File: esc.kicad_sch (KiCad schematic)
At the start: 58 parts, among them Q10 NMOS, Q5 NMOS, Q6 NMOS, Q7 NMOS, Q8 NMOS, Q9 NMOS, U16 DRV8328ARUYR, U20 STM32G071GBU6

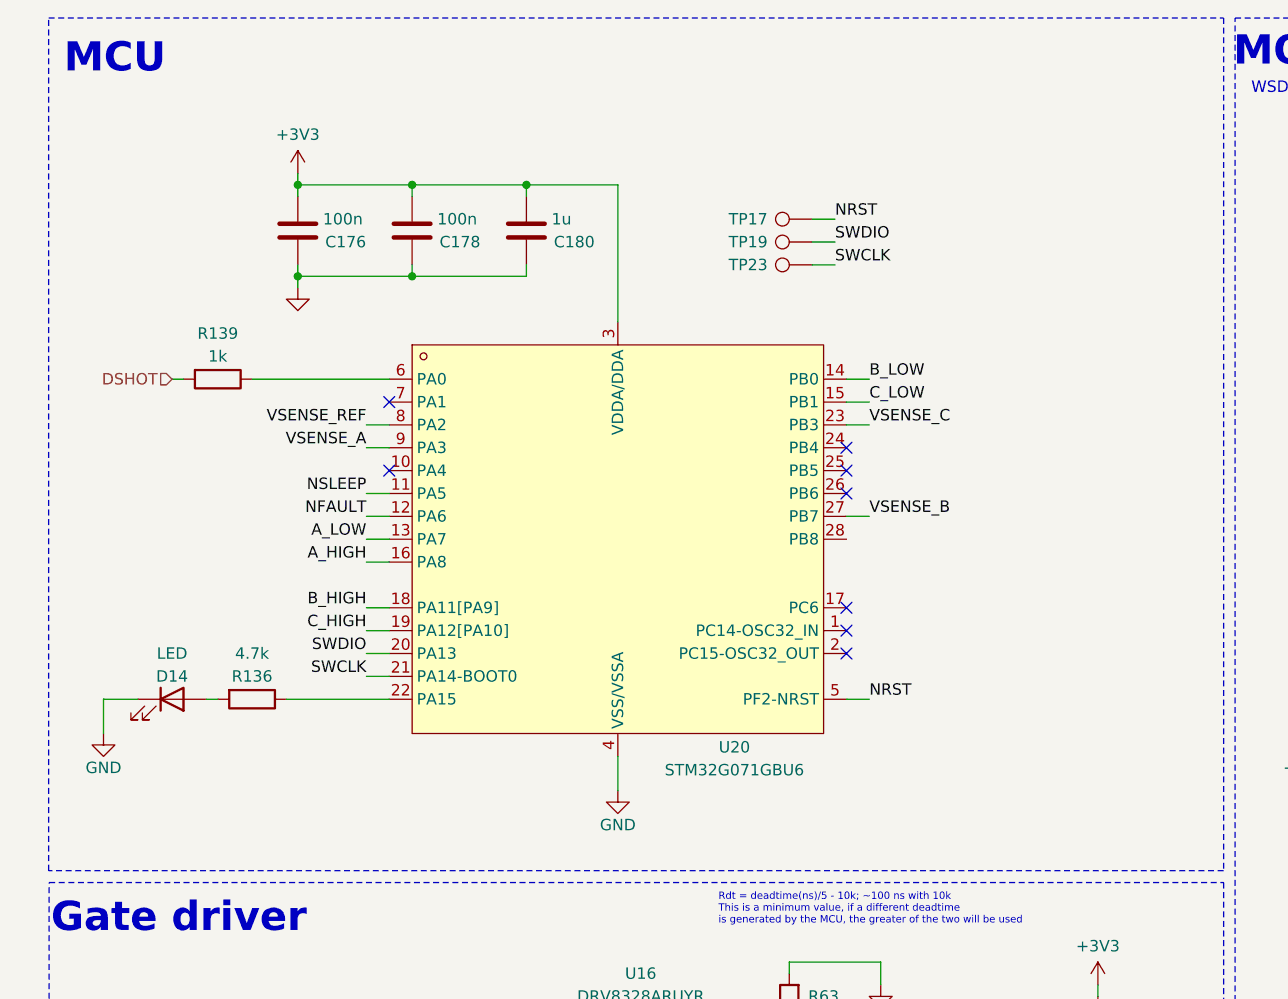
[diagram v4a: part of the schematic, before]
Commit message: Ostensibly finish V4 ESC layout
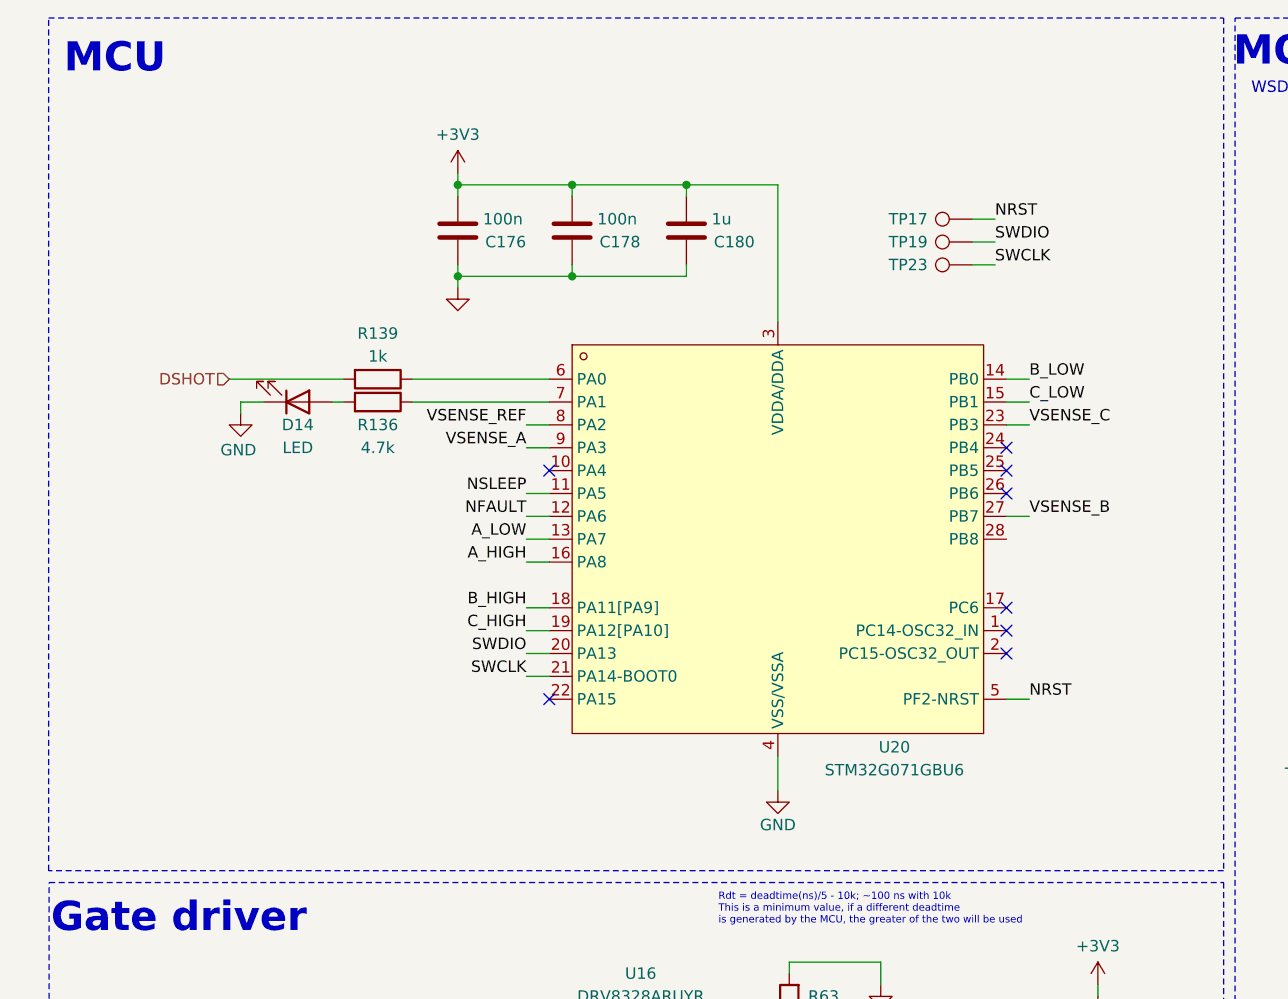
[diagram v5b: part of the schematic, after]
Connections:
- net at U20.22 (PA15): no longer R136.1
- net at U20.7 (PA1): now also R136.1
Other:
- moved on the sheet: C176, C178, C180, D14, R136, R139, TP17, TP19, TP23, U20

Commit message: Remove extra capacitors for now
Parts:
- removed C116, C118, C120, C122, C123, C124, C125, C202, C206: 10u, Capacitor_SMD:C_1206_3216Metric, symbol Device:C
- C113, C114, C121, C198: footprint Capacitor_SMD:C_1206_3216Metric -> Capacitor_SMD:C_1210_3225Metric
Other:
- moved on the sheet: C113, C114, C121, C198

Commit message: Group FC stuff
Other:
- note added: "1210 10uF caps from Samsung retain ~8 uF even at 3S LiHV Which results in ~32 uF total in the worst case scenario"
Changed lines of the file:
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@@
+		)
+	)
+	(text "1210 10uF caps from Samsung retain ~8 uF even at 3S LiHV\nWhich results in ~32 uF total in the worst case scenario"
+		(exclude_from_sim no)
+		(at 219.71 153.924 0)
+		(effects
+			(font
+				(size 1.27 1.27)
+			)
 		)
 	)

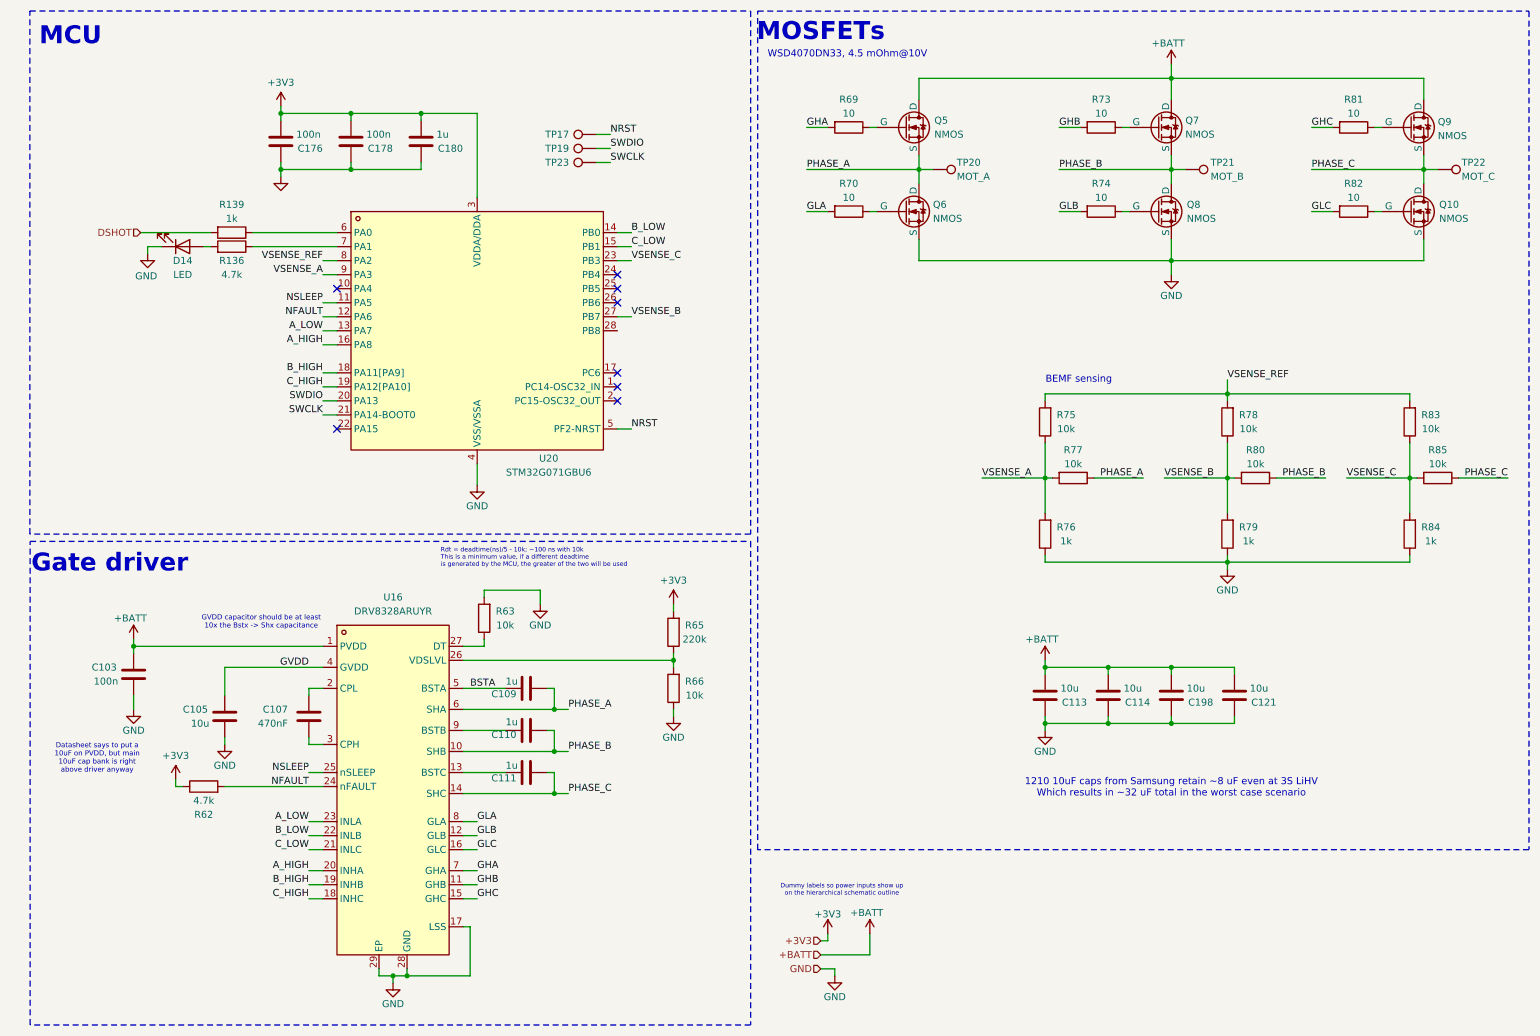
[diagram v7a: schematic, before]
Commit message: Fix BEMF comparator pinout
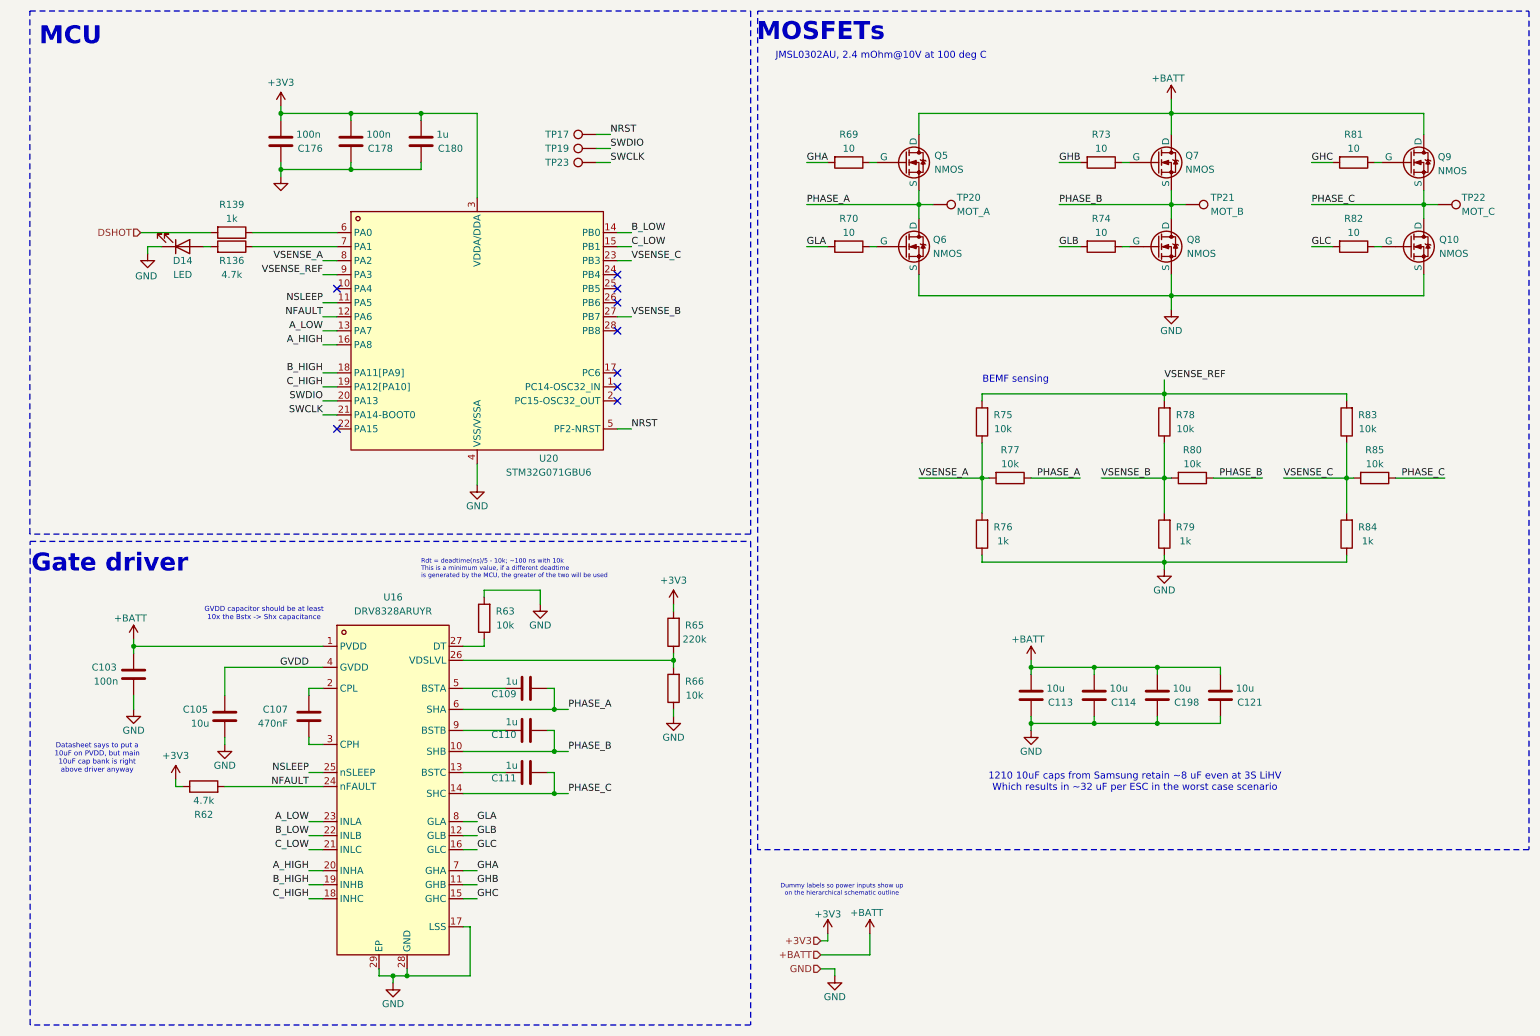
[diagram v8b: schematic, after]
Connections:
- net VSENSE_A: now also U20.8 (PA2); no longer U20.9 (PA3)
- net VSENSE_REF: now also U20.9 (PA3); no longer U20.8 (PA2)
- net BSTA: no longer names the net of C109.2, U16.5 (BSTA)
- no-connect marks 8 -> 9
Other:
- note added: "1210 10uF caps from Samsung retain ~8 uF even at 3S LiHV Which results in ~32 uF per ESC in the worst case scenario"
- note added: "JMSL0302AU, 2.4 mOhm@10V at 100 deg C"
- note removed: "1210 10uF caps from Samsung retain ~8 uF even at 3S LiHV Which results in ~32 uF total in the worst case scenario"
- note removed: "WSD4070DN33, 4.5 mOhm@10V"
- company: All-in-one drone flight controller, camera and ESC -> All-in-one drone flight controller, camera and 2S-3S ESC
- moved on the sheet: C113, C114, C121, C198, Q10, Q5, Q6, Q7, Q8, Q9, R69, R70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
